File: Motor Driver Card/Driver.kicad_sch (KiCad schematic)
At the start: 9 parts, among them M1 MD13B, Q1 2N3904

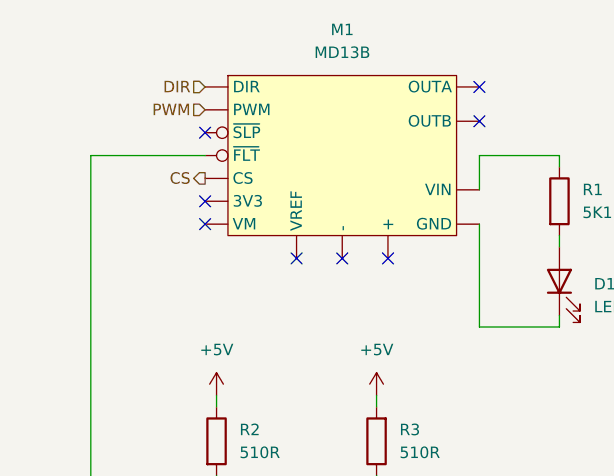
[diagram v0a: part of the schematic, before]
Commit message: Route motor driver card
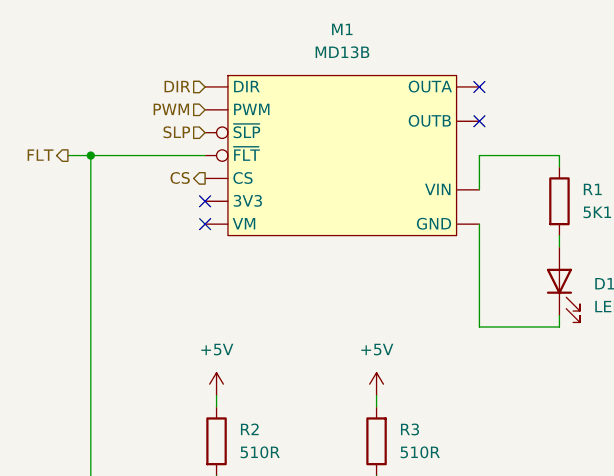
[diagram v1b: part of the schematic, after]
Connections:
- net FLT: now reaches D3.2 (A), M1.12 (~{FLT}), R2.2, R4.1
- net SLP: now reaches M1.11 (~{SLP})
- no-connect marks 8 -> 4
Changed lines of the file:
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@@
+	)
+	(junction
+		(at 74.93 80.01)
+		(diameter 0)
+		(color 0 0 0 0)
 	)
 	(junction
@@
 	)
 	(no_connect
-		(at 97.79 91.44)
-	)
-	(no_connect
 		(at 87.63 87.63)
 	)
@@
 	)
 	(no_connect
-		(at 107.95 91.44)
-	)
-	(no_connect
-		(at 87.63 77.47)
-	)
-	(no_connect
-		(at 102.87 91.44)
-	)
-	(no_connect
 		(at 118.11 72.39)
 	)
@@
 	(wire
 		(pts
+			(xy 72.39 80.01) (xy 74.93 80.01)
+		)
+		(stroke
+			(width 0)
+			(type default)
+		)
+	)
+	(wire
+		(pts
 			(xy 127 80.01) (xy 127 81.28)
 		)
@@
 	(wire
 		(pts
+			(xy 74.93 80.01) (xy 87.63 80.01)
+		)
+		(stroke
+			(width 0)
+			(type default)
+		)
+	)
+	(wire
+		(pts
 			(xy 97.79 124.46) (xy 99.06 124.46)
 		)
@@
 	(wire
 		(pts
-			(xy 74.93 80.01) (xy 87.63 80.01)
-		)
-		(stroke
-			(width 0)
-			(type default)
-		)
-	)
-	(wire
-		(pts
 			(xy 127 99.06) (xy 127 97.79)
 		)
@@
 			(width 0)
 			(type default)
+		)
+	)
+	(hierarchical_label "SLP"
+		(shape input)
+		(at 87.63 77.47 180)
+		(effects
+			(font
+				(size 1.27 1.27)
+			)
+			(justify right)
 		)
 	)
@@
 		(shape input)
 		(at 87.63 72.39 180)
+		(effects
+			(font
+				(size 1.27 1.27)
+			)
+			(justify right)
+		)
+	)
+	(hierarchical_label "FLT"
+		(shape output)
+		(at 72.39 80.01 180)
 		(effects
 			(font
@@
 		(pin "3"
 		)
-		(pin "6"
-		)
-		(pin "7"
-		)
 		(pin "2"
 		)
@@
 		(pin "1"
 		)
-		(pin "14"
-		)
 		(pin "12"

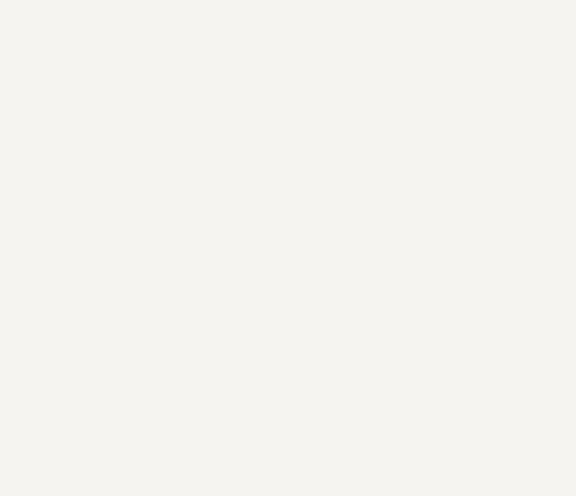
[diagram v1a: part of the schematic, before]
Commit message: Add thermistors to motor driver card
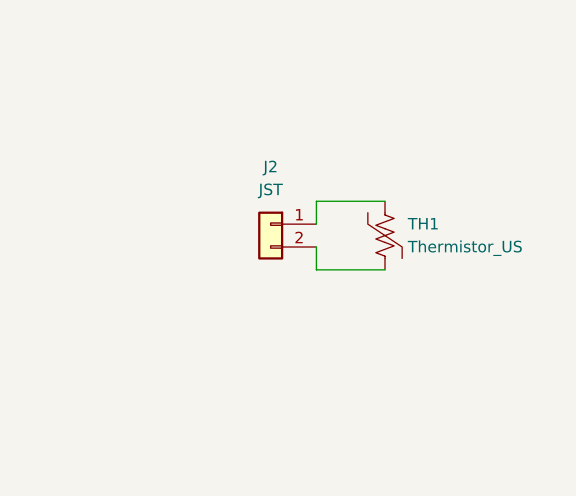
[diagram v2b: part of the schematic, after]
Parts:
- added J2: JST, Connector_PinHeader_2.54mm:PinHeader_1x02_P2.54mm_Vertical, symbol Connector_Generic:Conn_01x02
- added TH1: Thermistor_US, Resistor_THT:R_Axial_DIN0204_L3.6mm_D1.6mm_P2.54mm_Vertical, symbol Device:Thermistor_US
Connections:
- new net: J2.1 (Pin_1), TH1.1
- new net: J2.2 (Pin_2), TH1.2
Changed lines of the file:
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@@
+	(wire
+		(pts
+			(xy 179.07 92.71) (xy 171.45 92.71)
+		)
+		(stroke
+			(width 0)
+			(type default)
+		)
+	)
 	(wire
 		(pts
@@
 	(wire
 		(pts
+			(xy 179.07 85.09) (xy 171.45 85.09)
+		)
+		(stroke
+			(width 0)
+			(type default)
+		)
+	)
+	(wire
+		(pts
 			(xy 74.93 80.01) (xy 74.93 124.46)
+		)
+		(stroke
+			(width 0)
+			(type default)
+		)
+	)
+	(wire
+		(pts
+			(xy 171.45 92.71) (xy 171.45 90.17)
+		)
+		(stroke
+			(width 0)
+			(type default)
+		)
+	)
+	(wire
+		(pts
+			(xy 171.45 85.09) (xy 171.45 87.63)
 		)
 		(stroke
@@
 					(unit 1)
 				)
+			)
+		)
+	)
+	(symbol
+		(lib_id "Connector_Generic:Conn_01x02")
+		(at 166.37 87.63 0)
+		(mirror y)
+		(unit 1)
+		(exclude_from_sim no)
+		(in_bom yes)
+		(on_board yes)
+		(dnp no)
+		(fields_autoplaced yes)
+		(property "Reference" "J2"
+			(at 166.37 81.28 0)
+			(effects
+				(font
+					(size 1.27 1.27)
+				)
+			)
+		)
+		(property "Value" "JST"
+			(at 166.37 83.82 0)
+			(effects
+				(font
+					(size 1.27 1.27)
+				)
+			)
+		)
+		(property "Footprint" "Connector_PinHeader_2.54mm:PinHeader_1x02_P2.54mm_Vertical"
+			(at 166.37 87.63 0)
+			(effects
+				(font
+					(size 1.27 1.27)
+				)
+				(hide yes)
+			)
+		)
+		(property "Datasheet" "~"
+			(at 166.37 87.63 0)
+			(effects
+				(font
+					(size 1.27 1.27)
+				)
+				(hide yes)
+			)
+		)
+		(property "Description" "Generic connector, single row, 01x02, script generated (kicad-library-utils/schlib/autogen/connector/)"
+			(at 166.37 87.63 0)
+			(effects
+				(font
+					(size 1.27 1.27)
+				)
+				(hide yes)
+			)
+		)
+		(pin "2"
+		)
+		(pin "1"
+		)
+		(instances
+			(project ""
+				(path "/5aa4e8c2-4058-44c7-902b-84d41792a65b/086e49ea-d672-442a-9ce5-69c39153f8ee"
+					(reference "J2")
+					(unit 1)
+				)
+				(path "/5aa4e8c2-4058-44c7-902b-84d41792a65b/36ab9c78-7eb5-4a4f-b0c3-9a481581a7cf"
+					(reference "J3")
+					(unit 1)
+				)
+				(path "/5aa4e8c2-4058-44c7-902b-84d41792a65b/a2a4ecd6-3034-4225-8002-20f3d2522dde"
+					(reference "J5")
+					(unit 1)
+				)
+				(path "/5aa4e8c2-4058-44c7-902b-84d41792a65b/f33324f3-0309-453c-97d7-625409dd8a8e"
+					(reference "J4")
+					(unit 1)
+				)
+			)
+		)
+	)
+	(symbol
+		(lib_id "Device:Thermistor_US")
+		(at 179.07 88.9 0)
+		(unit 1)
+		(exclude_from_sim no)
+		(in_bom yes)
+		(on_board yes)
+		(dnp no)
+		(fields_autoplaced yes)
+		(property "Reference" "TH1"
+			(at 181.61 87.6299 0)
+			(effects
+				(font
+					(size 1.27 1.27)
+				)
+				(justify left)
+			)
+		)
+		(property "Value" "Thermistor_US"
+			(at 181.61 90.1699 0)
+			(effects
+				(font
+					(size 1.27 1.27)
+				)
+				(justify left)
+			)
+		)
+		(property "Footprint" "Resistor_THT:R_Axial_DIN0204_L3.6mm_D1.6mm_P2.54mm_Vertical"
+			(at 179.07 88.9 0)
+			(effects
+				(font
+					(size 1.27 1.27)
+				)
+				(hide yes)
+			)
+		)
+		(property "Datasheet" "~"
+			(at 179.07 88.9 0)
+			(effects
+				(font
+					(size 1.27 1.27)
+				)
+				(hide yes)
+			)
+		)
+		(property "Description" "Thermistor, temperature dependent resistor, US symbol"
+			(at 179.07 88.9 0)
+			(effects
+				(font
+					(size 1.27 1.27)
+				)
+				(hide yes)
+			)
+		)
+		(pin "2"
+		)
+		(pin "1"
+		)
+		(instances
+			(project ""
+				(path "/5aa4e8c2-4058-44c7-902b-84d41792a65b/086e49ea-d672-442a-9ce5-69c39153f8ee"
+					(reference "TH1")
+					(unit 1)
+				)
+				(path "/5aa4e8c2-4058-44c7-902b-84d41792a65b/36ab9c78-7eb5-4a4f-b0c3-9a481581a7cf"
+					(reference "TH2")
+					(unit 1)
+				)
+				(path "/5aa4e8c2-4058-44c7-902b-84d41792a65b/a2a4ecd6-3034-4225-8002-20f3d2522dde"
+					(reference "TH4")
+					(unit 1)
+				)
+				(path "/5aa4e8c2-4058-44c7-902b-84d41792a65b/f33324f3-0309-453c-97d7-625409dd8a8e"
+					(reference "TH3")
+					(unit 1)
+				)

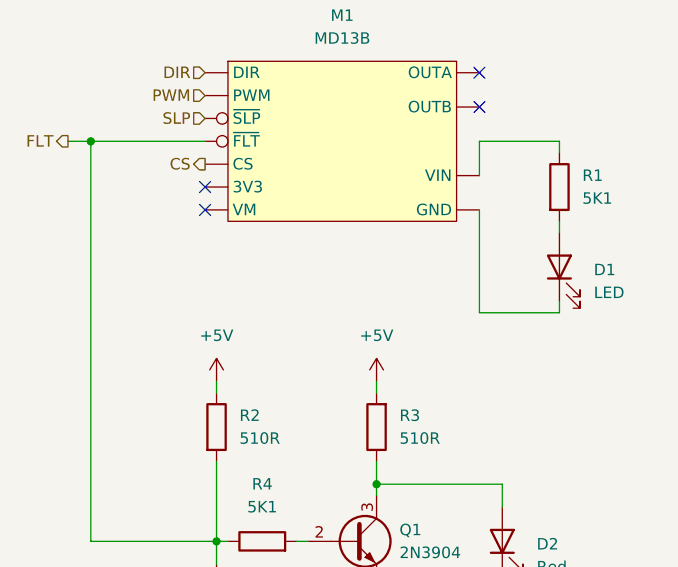
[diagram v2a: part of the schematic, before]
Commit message: Last-minute changes for pico GPIO voltage levels
Adjusted MDCB to work in 3.3v rather than 5v to not blow up a pico. Thankfully we have a readily available 3.3v source from the motor drivers themselves.
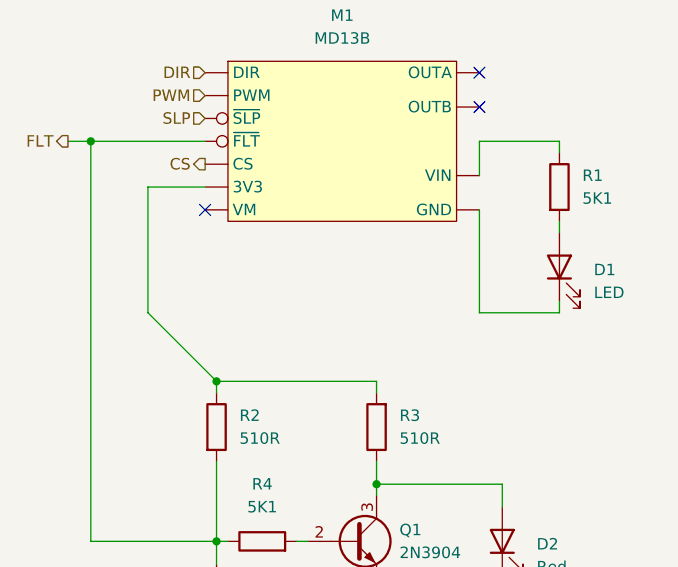
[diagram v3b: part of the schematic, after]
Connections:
- net +5V is gone; now on an unnamed net: R2.1, R3.2
- no-connect marks 4 -> 3

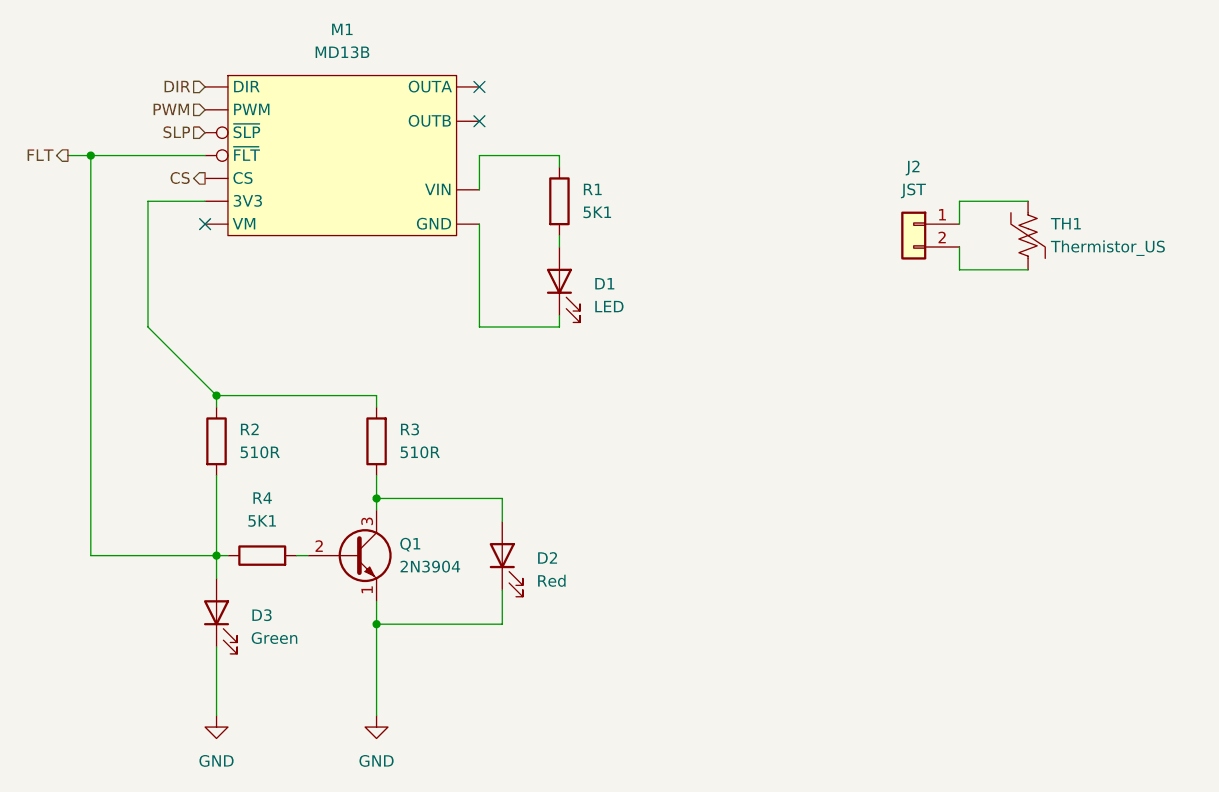
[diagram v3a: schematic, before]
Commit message: Updated PCB designs across the motor driver, analog board, and PDB
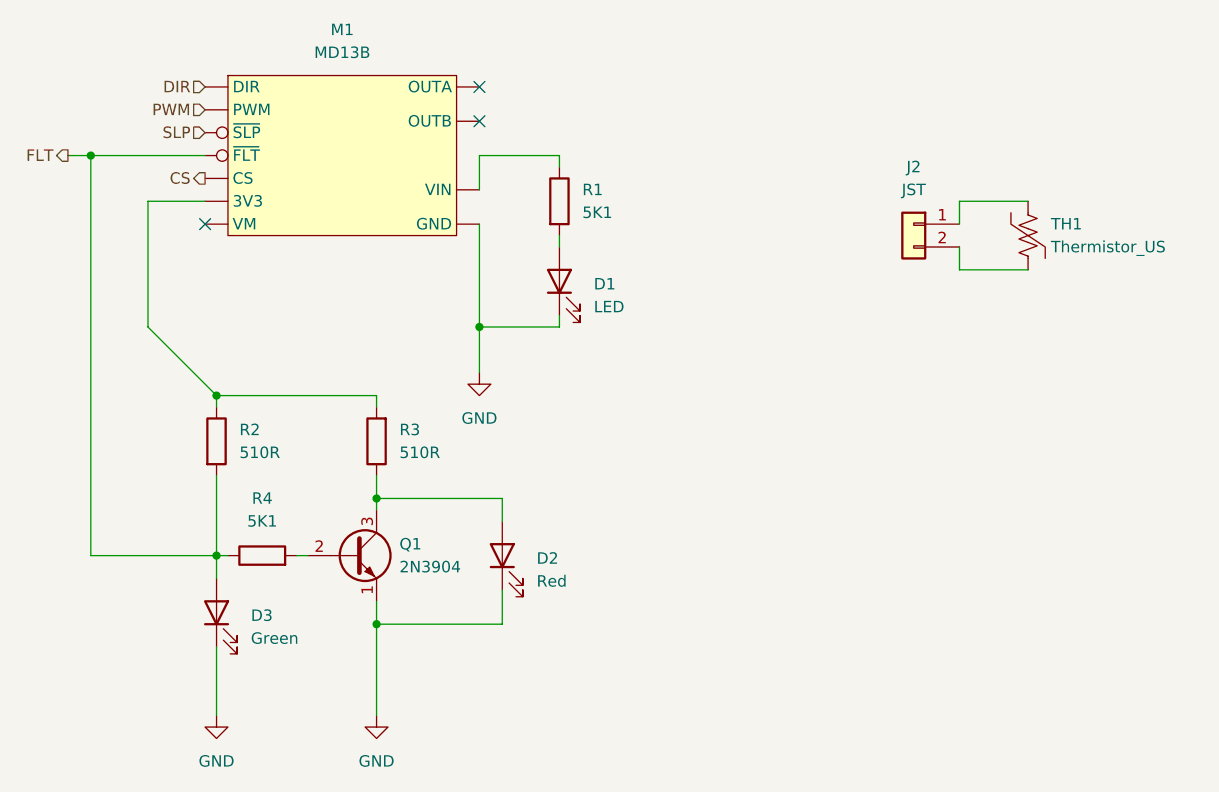
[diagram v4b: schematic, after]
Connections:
- net GND: now also D1.1 (K), M1.2 (GND)
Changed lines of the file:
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@@
+	)
+	(junction
+		(at 118.11 99.06)
+		(diameter 0)
+		(color 0 0 0 0)
 	)
 	(junction
@@
 		(pts
 			(xy 90.17 124.46) (xy 88.9 124.46)
+		)
+		(stroke
+			(width 0)
+			(type default)
+		)
+	)
+	(wire
+		(pts
+			(xy 118.11 104.14) (xy 118.11 99.06)
 		)
 		(stroke
@@
 					(unit 1)
 				)
+			)
+		)
+	)
+	(symbol
+		(lib_id "power:GND")
+		(at 118.11 104.14 0)
+		(unit 1)
+		(body_style 1)
+		(exclude_from_sim no)
+		(in_bom yes)
+		(on_board yes)
+		(in_pos_files yes)
+		(dnp no)
+		(fields_autoplaced yes)
+		(property "Reference" "#PWR09"
+			(at 118.11 110.49 0)
+			(hide yes)
+			(show_name no)
+			(do_not_autoplace no)
+			(effects
+				(font
+					(size 1.27 1.27)
+				)
+			)
+		)
+		(property "Value" "GND"
+			(at 118.11 109.22 0)
+			(show_name no)
+			(do_not_autoplace no)
+			(effects
+				(font
+					(size 1.27 1.27)
+				)
+			)
+		)
+		(property "Footprint" ""
+			(at 118.11 104.14 0)
+			(hide yes)
+			(show_name no)
+			(do_not_autoplace no)
+			(effects
+				(font
+					(size 1.27 1.27)
+				)
+			)
+		)
+		(property "Datasheet" ""
+			(at 118.11 104.14 0)
+			(hide yes)
+			(show_name no)
+			(do_not_autoplace no)
+			(effects
+				(font
+					(size 1.27 1.27)
+				)
+			)
+		)
+		(property "Description" "Power symbol creates a global label with name \"GND\" , ground"
+			(at 118.11 104.14 0)
+			(hide yes)
+			(show_name no)
+			(do_not_autoplace no)
+			(effects
+				(font
+					(size 1.27 1.27)
+				)
+			)
+		)
+		(pin "1"
+		)
+		(instances
+			(project "Motor_Driver_Card"
+				(path "/5aa4e8c2-4058-44c7-902b-84d41792a65b/086e49ea-d672-442a-9ce5-69c39153f8ee"
+					(reference "#PWR09")
+					(unit 1)
+				)
+				(path "/5aa4e8c2-4058-44c7-902b-84d41792a65b/36ab9c78-7eb5-4a4f-b0c3-9a481581a7cf"
+					(reference "#PWR010")
+					(unit 1)
+				)
+				(path "/5aa4e8c2-4058-44c7-902b-84d41792a65b/a2a4ecd6-3034-4225-8002-20f3d2522dde"
+					(reference "#PWR014")
+					(unit 1)
+				)
+				(path "/5aa4e8c2-4058-44c7-902b-84d41792a65b/f33324f3-0309-453c-97d7-625409dd8a8e"
+					(reference "#PWR013")
+					(unit 1)
+				)
